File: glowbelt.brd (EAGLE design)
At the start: 40.3 x 24.8 mm, 12 parts, among them IC1 TINY10S

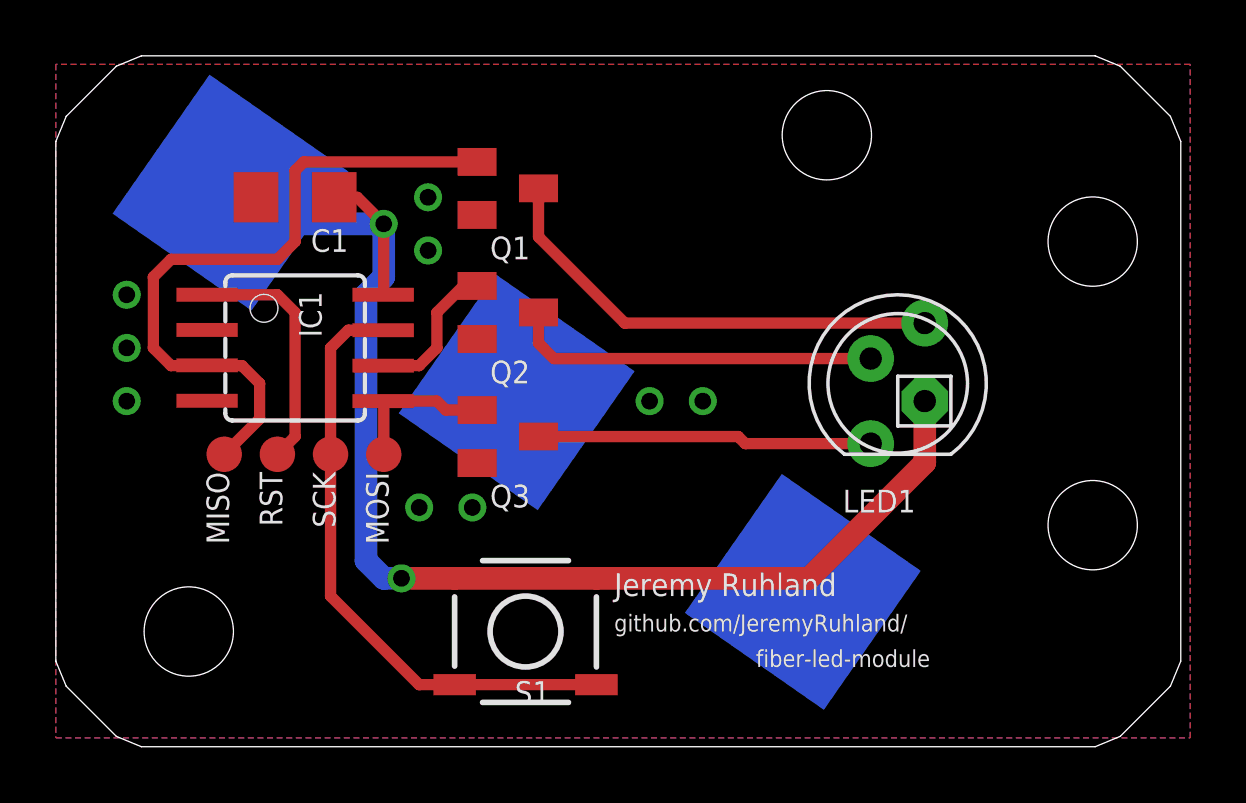
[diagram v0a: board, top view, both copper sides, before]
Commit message: added optional current limiting resistor array
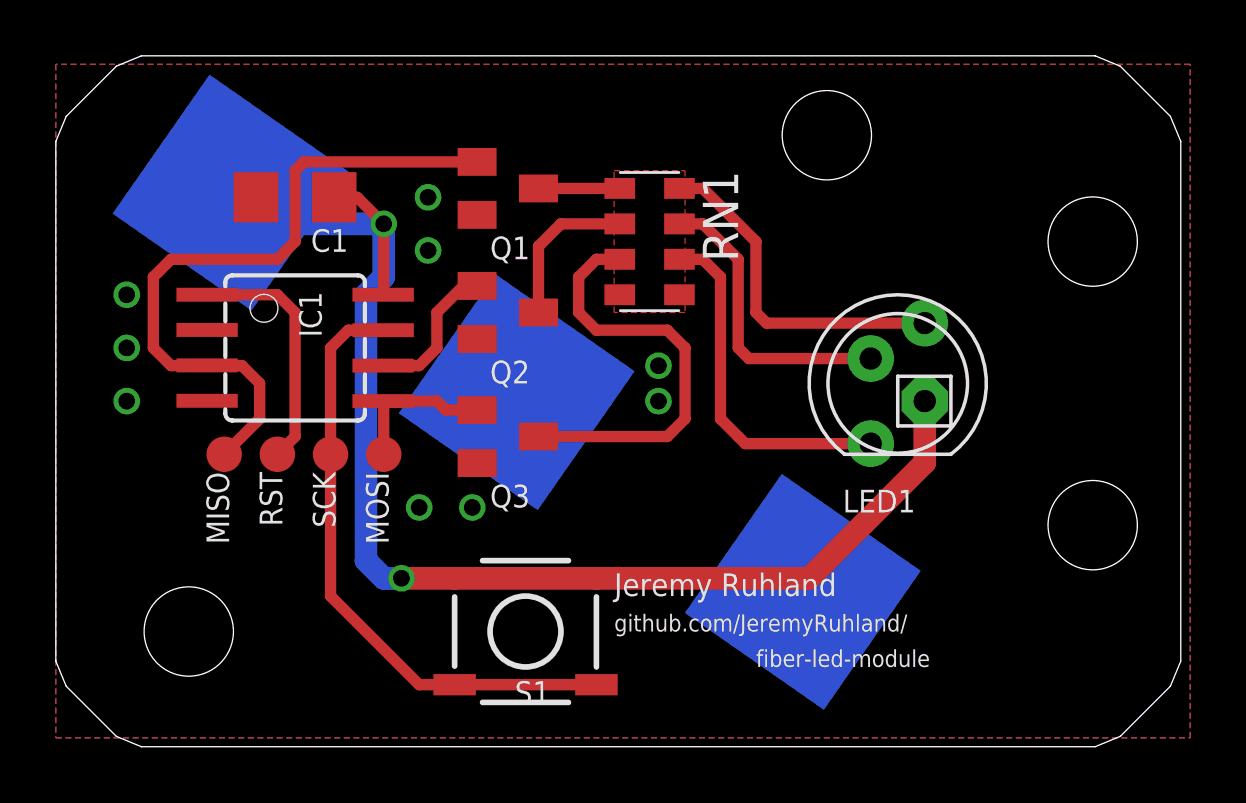
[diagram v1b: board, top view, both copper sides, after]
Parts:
- added RN1: (no value), resistor-dil:EXBS8V
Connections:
- removed net N$10: LED1.1, Q3.3
- removed net N$8: LED1.4, Q1.3
- removed net N$9: LED1.3, Q2.3
- new net N$2: Q1.3, RN1.1
- new net N$3: Q2.3, RN1.2
- new net N$4: Q3.3, RN1.3
- new net N$5: LED1.3, RN1.7
- new net N$6: LED1.4, RN1.8
- new net N$7: LED1.1, RN1.6
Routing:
- net N$8: track 16.9 -> 0.00 mm
- net N$4: track 0.00 -> 15.4 mm
- net N$9: track 13.2 -> 0.00 mm
- net N$7: track 0.00 -> 12.6 mm
- net N$6: track 0.00 -> 12.3 mm
- net N$10: track 12.0 -> 0.00 mm
- net N$5: track 0.00 -> 10.7 mm
- net N$3: track 0.00 -> 5.61 mm
- net N$2: track 0.00 -> 2.91 mm
- added copper zone on layer 1, net N$8
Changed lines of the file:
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@@
 <setting verticaltext="up"/>
 </settings>
-<grid distance="0.05" unitdist="inch" unit="inch" style="lines" multiple="1" display="no" altdistance="0.025" altunitdist="inch" altunit="inch"/>
+<grid distance="0.05" unitdist="inch" unit="inch" style="lines" multiple="1" display="no" altdistance="0.0125" altunitdist="inch" altunit="inch"/>
 <layers>
 <layer number="1" name="Top" color="4" fill="1" visible="yes" active="yes"/>
@@
 Einstellungen hier und speichern die Design Rules unter
 einem neuen Namen ab.</description>
-<description language="en">&lt;b&gt;EAGLE Design Rules&lt;/b&gt;
+<description language="en">&lt;b&gt;Laen's PCB Order Design Rules&lt;/b&gt;
 &lt;p&gt;
-The default Design Rules have been set to cover
-a wide range of applications. Your particular design
-may have different requirements, so please make the
-necessary adjustments and save your customized
-design rules under a new name.</description>
+Please make sure your boards conform to these design rules.</description>
 <param name="layerSetup" value="(1*16)"/>
-<param name="mtCopper" value="0.035mm 0.035mm 0.035mm 0.035mm 0.035mm 0.035mm 0.035mm 0.035mm 0.035mm 0.035mm 0.035mm 0.035mm 0.035mm 0.035mm 0.035mm 0.035mm"/>
-<param name="mtIsolate" value="1.5mm 0.15mm 0.2mm 0.15mm 0.2mm 0.15mm 0.2mm 0.15mm 0.2mm 0.15mm 0.2mm 0.15mm 0.2mm 0.15mm 0.2mm"/>
-<param name="mdWireWire" value="8mil"/>
-<param name="mdWirePad" value="8mil"/>
-<param name="mdWireVia" value="8mil"/>
-<param name="mdPadPad" value="8mil"/>
-<param name="mdPadVia" value="8mil"/>
-<param name="mdViaVia" value="8mil"/>
-<param name="mdSmdPad" value="8mil"/>
-<param name="mdSmdVia" value="8mil"/>
-<param name="mdSmdSmd" value="8mil"/>
+<param name="mtCopper" value="0.0356mm 0.0356mm 0.0356mm 0.0356mm 0.0356mm 0.0356mm 0.0356mm 0.0356mm 0.0356mm 0.0356mm 0.0356mm 0.0356mm 0.0356mm 0.0356mm 0.0356mm 0.0356mm"/>
+<param name="mtIsolate" value="1.5011mm 0.1499mm 0.2007mm 0.1499mm 0.2007mm 0.1499mm 0.2007mm 0.1499mm 0.2007mm 0.1499mm 0.2007mm 0.1499mm 0.2007mm 0.1499mm 0.2007mm"/>
+<param name="mdWireWire" value="6mil"/>
+<param name="mdWirePad" value="6mil"/>
+<param name="mdWireVia" value="6mil"/>
+<param name="mdPadPad" value="6mil"/>
+<param name="mdPadVia" value="6mil"/>
+<param name="mdViaVia" value="6mil"/>
+<param name="mdSmdPad" value="6mil"/>
+<param name="mdSmdVia" value="6mil"/>
+<param name="mdSmdSmd" value="6mil"/>
 <param name="mdViaViaSameLayer" value="8mil"/>
 <param name="mnLayersViaInSmd" value="2"/>
-<param name="mdCopperDimension" value="40mil"/>
-<param name="mdDrill" value="8mil"/>
+<param name="mdCopperDimension" value="15mil"/>
+<param name="mdDrill" value="6mil"/>
 <param name="mdSmdStop" value="0mil"/>
-<param name="msWidth" value="10mil"/>
-<param name="msDrill" value="24mil"/>
-<param name="msMicroVia" value="9.99mm"/>
+<param name="msWidth" value="6mil"/>
+<param name="msDrill" value="13mil"/>
+<param name="msMicroVia" value="13mil"/>
 <param name="msBlindViaRatio" value="0.5"/>
 <param name="rvPadTop" value="0.25"/>
@@
 <param name="rvMicroViaOuter" value="0.25"/>
 <param name="rvMicroViaInner" value="0.25"/>
-<param name="rlMinPadTop" value="10mil"/>
+<param name="rlMinPadTop" value="7mil"/>
 <param name="rlMaxPadTop" value="20mil"/>
-<param name="rlMinPadInner" value="10mil"/>
+<param name="rlMinPadInner" value="7mil"/>
 <param name="rlMaxPadInner" value="20mil"/>
-<param name="rlMinPadBottom" value="10mil"/>
+<param name="rlMinPadBottom" value="7mil"/>
 <param name="rlMaxPadBottom" value="20mil"/>
-<param name="rlMinViaOuter" value="8mil"/>
+<param name="rlMinViaOuter" value="7mil"/>
 <param name="rlMaxViaOuter" value="20mil"/>
-<param name="rlMinViaInner" value="8mil"/>
+<param name="rlMinViaInner" value="7mil"/>
 <param name="rlMaxViaInner" value="20mil"/>
 <param name="rlMinMicroViaOuter" value="4mil"/>
@@
 <attribute name="NAME" x="31.115" y="8.89" size="0.8128" layer="21" font="vector" rot="R180"/>
 </element>
+<element name="RN1" library="resistor-dil" package="EXBS8V" value="" x="21.59" y="17.78" rot="R270">
+<attribute name="OC_NEWARK" value="unknown" x="21.59" y="17.78" size="1.778" layer="27" rot="R270" display="off"/>
+<attribute name="MPN" value="" x="21.59" y="17.78" size="1.778" layer="27" rot="R270" display="off"/>
+<attribute name="MF" value="" x="21.59" y="17.78" size="1.778" layer="27" rot="R270" display="off"/>
+<attribute name="OC_FARNELL" value="unknown" x="21.59" y="17.78" size="1.778" layer="27" rot="R270" display="off"/>
+</element>
 </elements>
 <signals>
@@
 <via x="13.6525" y="19.3675" extent="1-16" drill="0.6"/>
 <via x="13.6525" y="17.4625" extent="1-16" drill="0.6"/>
-<via x="23.495" y="12.065" extent="1-16" drill="0.6"/>
-<via x="21.59" y="12.065" extent="1-16" drill="0.6"/>
+<via x="21.9075" y="12.065" extent="1-16" drill="0.6"/>
+<via x="21.9075" y="13.335" extent="1-16" drill="0.6"/>
 <via x="15.24" y="8.255" extent="1-16" drill="0.6"/>
 <via x="13.335" y="8.255" extent="1-16" drill="0.6"/>
@@
 <wire x1="14.605" y1="1.905" x2="13.335" y2="1.905" width="0.4064" layer="1"/>
 </signal>
-<signal name="N$8">
-<contactref element="Q1" pad="3"/>
-<contactref element="LED1" pad="4"/>
-<wire x1="31.4484" y1="14.859" x2="20.701" y2="14.859" width="0.4064" layer="1"/>
-<wire x1="20.701" y1="14.859" x2="17.61" y2="17.95" width="0.4064" layer="1"/>
-<wire x1="17.61" y1="19.685" x2="17.61" y2="17.95" width="0.4064" layer="1"/>
-</signal>
-<signal name="N$9">
-<contactref element="Q2" pad="3"/>
-<contactref element="LED1" pad="3"/>
-<wire x1="17.61" y1="15.24" x2="17.61" y2="14.14" width="0.4064" layer="1"/>
-<wire x1="17.61" y1="14.14" x2="17.78" y2="13.97" width="0.4064" layer="1"/>
-<wire x1="29.5116" y1="13.589" x2="18.161" y2="13.589" width="0.4064" layer="1"/>
-<wire x1="18.161" y1="13.589" x2="17.78" y2="13.97" width="0.4064" layer="1"/>
-</signal>
-<signal name="N$10">
-<contactref element="Q3" pad="3"/>
-<contactref element="LED1" pad="1"/>
-<wire x1="17.61" y1="10.795" x2="24.765" y2="10.795" width="0.4064" layer="1"/>
-<wire x1="29.5116" y1="10.541" x2="25.019" y2="10.541" width="0.4064" layer="1"/>
-<wire x1="25.019" y1="10.541" x2="24.765" y2="10.795" width="0.4064" layer="1"/>
-</signal>
 <signal name="N$1">
 <contactref element="IC1" pad="6"/>
@@
 <wire x1="14.92" y1="16.19" x2="13.97" y2="15.24" width="0.4064" layer="1"/>
 </signal>
+<signal name="N$2">
+<contactref element="Q1" pad="3"/>
+<contactref element="RN1" pad="1"/>
+<wire x1="17.61" y1="19.685" x2="20.52" y2="19.685" width="0.4064" layer="1"/>
+</signal>
+<signal name="N$3">
+<contactref element="Q2" pad="3"/>
+<contactref element="RN1" pad="2"/>
+<wire x1="17.61" y1="15.24" x2="17.61" y2="17.61" width="0.4064" layer="1"/>
+<wire x1="17.61" y1="17.61" x2="18.415" y2="18.415" width="0.4064" layer="1"/>
+<wire x1="18.415" y1="18.415" x2="20.52" y2="18.415" width="0.4064" layer="1"/>
+</signal>
+<signal name="N$4">
+<contactref element="Q3" pad="3"/>
+<contactref element="RN1" pad="3"/>
+<wire x1="17.61" y1="10.795" x2="22.225" y2="10.795" width="0.4064" layer="1"/>
+<wire x1="22.225" y1="10.795" x2="22.86" y2="11.43" width="0.4064" layer="1"/>
+<wire x1="22.86" y1="11.43" x2="22.86" y2="13.97" width="0.4064" layer="1"/>
+<wire x1="22.86" y1="13.97" x2="22.225" y2="14.605" width="0.4064" layer="1"/>
+<wire x1="22.225" y1="14.605" x2="19.685" y2="14.605" width="0.4064" layer="1"/>
+<wire x1="19.685" y1="14.605" x2="19.05" y2="15.24" width="0.4064" layer="1"/>
+<wire x1="19.05" y1="15.24" x2="19.05" y2="16.51" width="0.4064" layer="1"/>
+<wire x1="19.05" y1="16.51" x2="19.685" y2="17.145" width="0.4064" layer="1"/>
+<wire x1="19.685" y1="17.145" x2="20.52" y2="17.145" width="0.4064" layer="1"/>
+</signal>
+<signal name="N$5">
+<contactref element="RN1" pad="7"/>
+<contactref element="LED1" pad="3"/>
+<wire x1="29.5116" y1="13.589" x2="25.146" y2="13.589" width="0.4064" layer="1"/>
+<wire x1="25.146" y1="13.589" x2="24.765" y2="13.97" width="0.4064" layer="1"/>
+<wire x1="24.765" y1="13.97" x2="24.765" y2="17.145" width="0.4064" layer="1"/>
+<wire x1="24.765" y1="17.145" x2="23.495" y2="18.415" width="0.4064" layer="1"/>
+<wire x1="23.495" y1="18.415" x2="22.66" y2="18.415" width="0.4064" layer="1"/>
+</signal>
+<signal name="N$6">
+<contactref element="RN1" pad="8"/>
+<contactref element="LED1" pad="4"/>
+<wire x1="31.4484" y1="14.859" x2="25.781" y2="14.859" width="0.4064" layer="1"/>
+<wire x1="25.781" y1="14.859" x2="25.4" y2="15.24" width="0.4064" layer="1"/>
+<wire x1="25.4" y1="15.24" x2="25.4" y2="17.78" width="0.4064" layer="1"/>
+<wire x1="25.4" y1="17.78" x2="23.495" y2="19.685" width="0.4064" layer="1"/>
+<wire x1="23.495" y1="19.685" x2="22.66" y2="19.685" width="0.4064" layer="1"/>
+</signal>
+<signal name="N$7">
+<contactref element="RN1" pad="6"/>
+<contactref element="LED1" pad="1"/>
+<wire x1="22.66" y1="17.145" x2="23.495" y2="17.145" width="0.4064" layer="1"/>
+<wire x1="23.495" y1="17.145" x2="24.13" y2="16.51" width="0.4064" layer="1"/>
+<wire x1="24.13" y1="16.51" x2="24.13" y2="11.43" width="0.4064" layer="1"/>
+<wire x1="24.13" y1="11.43" x2="24.765" y2="10.795" width="0.4064" layer="1"/>
+<wire x1="29.5116" y1="10.541" x2="25.019" y2="10.541" width="0.4064" layer="1"/>
+<wire x1="25.019" y1="10.541" x2="24.765" y2="10.795" width="0.4064" layer="1"/>
+</signal>
+<signal name="N$8">
+<polygon width="0" layer="1" pour="cutout">
+<vertex x="20.32" y="20.32"/>
+<vertex x="22.86" y="20.32"/>
+<vertex x="22.86" y="15.24"/>
+<vertex x="20.32" y="15.24"/>
+</polygon>
+</signal>
 </signals>
